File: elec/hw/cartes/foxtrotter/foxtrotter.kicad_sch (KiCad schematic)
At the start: 28 parts, among them J1 22053061, U1 ADXRS453BRGZ, U2 SCH16T-K01-10

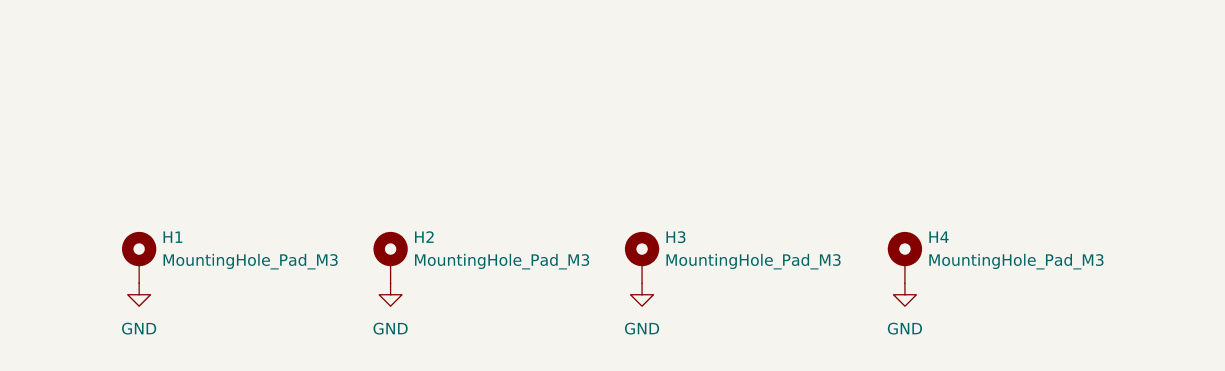
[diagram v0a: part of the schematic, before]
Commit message: foxtrotter : mounting holes changed to M2
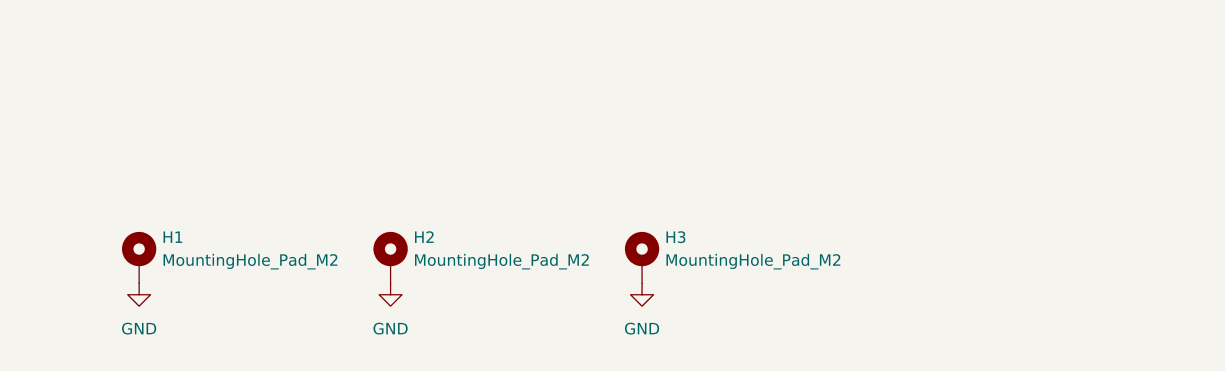
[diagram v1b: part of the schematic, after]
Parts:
- removed H4: MountingHole_Pad_M3, cocotter_others:MountingHole_3.2mm_M3_Pad_Via, symbol cocotter_others:MountingHole_Pad_M3
- H1, H2, H3: value MountingHole_Pad_M3 -> MountingHole_Pad_M2; footprint cocotter_others:MountingHole_3.2mm_M3_Pad_Via -> cocotter_others:MountingHole_2.2mm_M2_Pad_Via; symbol cocotter_others:MountingHole_Pad_M3 -> cocotter_others:MountingHole_Pad_M2

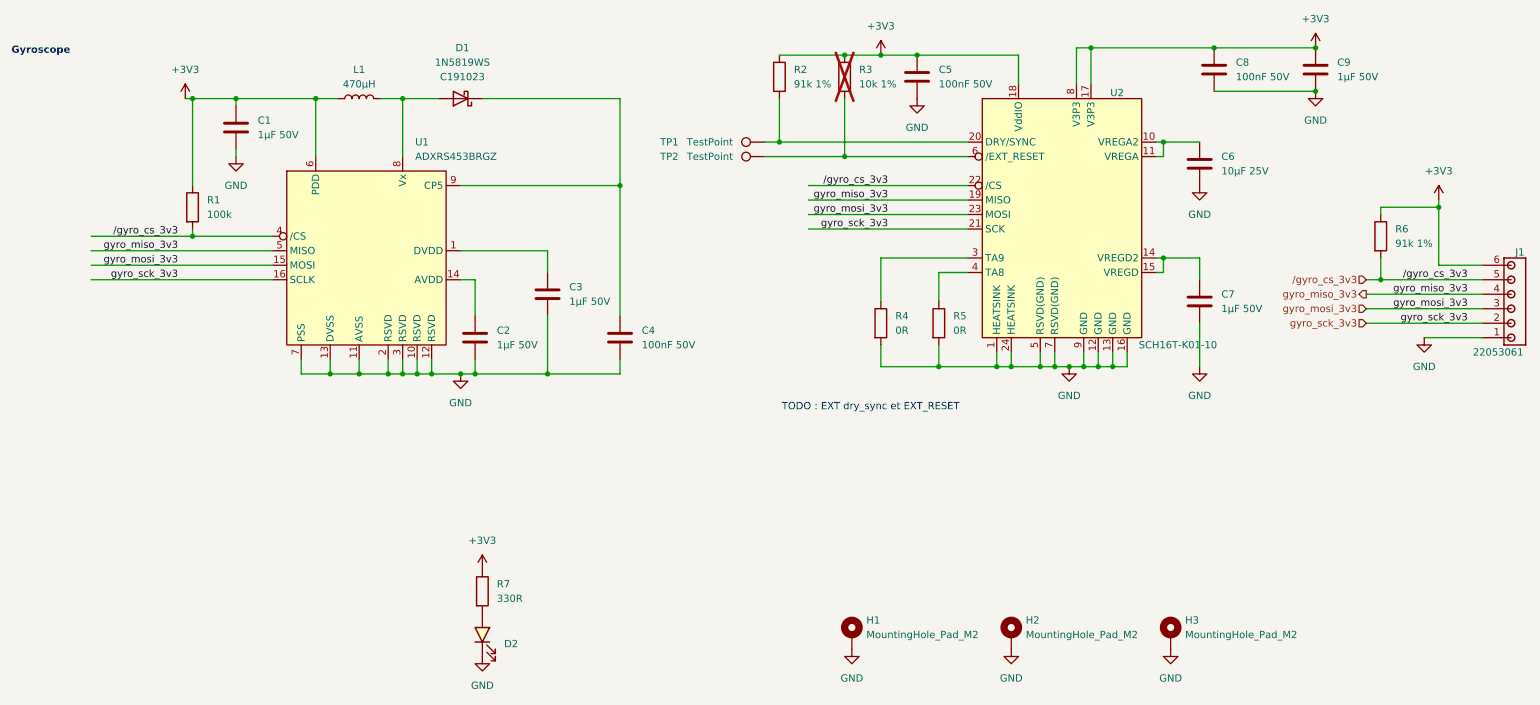
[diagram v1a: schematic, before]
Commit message: foxtrotter board updated with jlcpcb parts
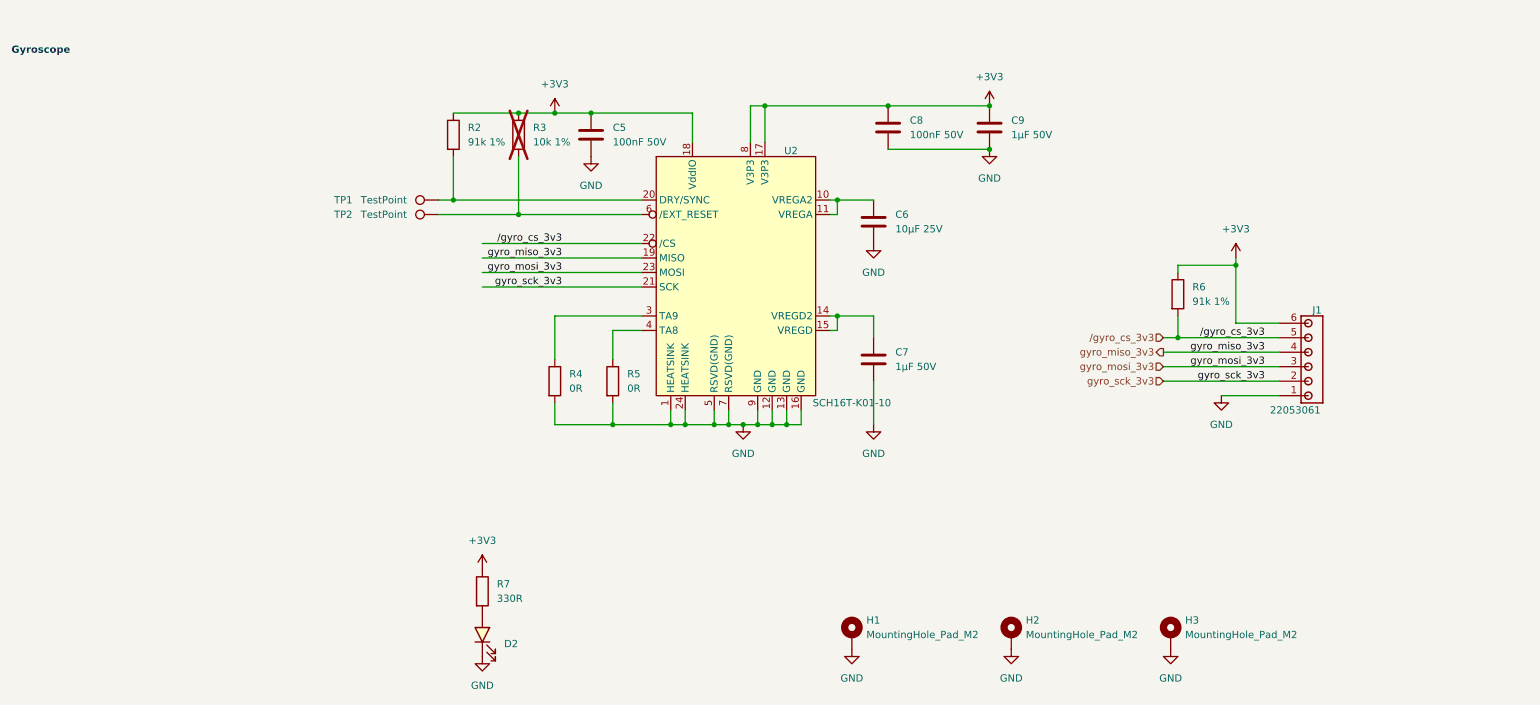
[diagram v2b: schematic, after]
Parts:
- removed C1, C2, C3: 1µF 50V, cocotter_capacitors:C_0805_2012Metric, symbol cocotter_capacitors:C_1µF_50V_0805
- removed C4: 100nF 50V, cocotter_capacitors:C_0603_1608Metric, symbol cocotter_capacitors:C_100nF_50V_0603
- removed D1: 1N5819WS, cocotter_diodes:D_SOD-323, symbol cocotter_diodes:1N5819WS
- removed L1: 470µH, cocotter_inductors:L_Kyocera_07A7_7.3x6.6mm, symbol cocotter_inductors:B82422H1474J
- removed R1: 100k, cocotter_resistor:r0603_reflow, symbol cocotter_resistors:R_100k_0603_1%
- removed U1: ADXRS453BRGZ, cocotter_ic:SOIC-16W_7.5x10.3mm_P1.27mm, symbol cocotter_ic:ADXRS453BRGZ
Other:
- note removed: "TODO : EXT dry_sync et EXT_RESET"
- moved on the sheet: C5, C6, C7, C8, C9, J1, R2, R3, R4, R5, R6, TP1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
